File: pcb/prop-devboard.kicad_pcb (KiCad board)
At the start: 4 copper layers, 50.8 x 22.9 mm, 41 parts, among them CN1 STDC14, CN2 SM04B-SRSS-TB (LF)(SN), CN3 ZX-PH2.0-WT2P, CN4 SM04B-SRSS-TB (LF)(SN), J1 Conn_01x12, J2 Conn_01x16, J3 GT-USB-7010ASV, Q1 DMG3415U-7, SW1 SW_Push, U1 STM32G0B1CBT6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

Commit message: Added CubeMX template, and more schematics work
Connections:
- CN1 pad 11: unconnected-(CN1-GNDD-Pad11) -> GND
- CN1 pad 12: unconnected-(CN1-~{RST}-Pad12) -> NRST
- CN1 pad 13: unconnected-(CN1-VCP_RX-Pad13) -> UART_RX
- CN1 pad 14: unconnected-(CN1-VCP_TX-Pad14) -> UART_TX
- CN1 pad 2: unconnected-(CN1-GND-Pad2) -> GND
- CN1 pad 3: unconnected-(CN1-VCC-Pad3) -> +3V3
- CN1 pad 4: unconnected-(CN1-SWDIO-Pad4) -> SWDIO
- CN1 pad 5: unconnected-(CN1-GND-Pad5) -> GND
- CN1 pad 6: unconnected-(CN1-SWCLK-Pad6) -> SWCLK
- CN2 pad 1: unconnected-(CN2-Pad1) -> GND
- CN2 pad 2: unconnected-(CN2-Pad2) -> +3V3
- CN2 pad 3: unconnected-(CN2-Pad3) -> I2C1_SDA
- CN2 pad 4: unconnected-(CN2-Pad4) -> I2C1_SCL
- CN4 pad 1: unconnected-(CN4-Pad1) -> GND
- CN4 pad 2: unconnected-(CN4-Pad2) -> +3V3
- CN4 pad 3: unconnected-(CN4-Pad3) -> I2C2_SDA
- CN4 pad 4: unconnected-(CN4-Pad4) -> I2C2_SCL
- U1 pad 30: unconnected-(U1-PC6-Pad30) -> UART_TX
- U1 pad 31: unconnected-(U1-PC7-Pad31) -> UART_RX

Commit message: Lots of work on schematics
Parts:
- added D2: ESDA7P60-1U1M, prop-devboard:D1610-RD, F.Cu at (115.7, 95.5)
- added D4: ESDALC6V1W5, prop-devboard:SOT-323-5_L2.0-W1.3-LS2.1-BL, F.Cu at (135.4, 85.5)
- moved C10 5.01 mm to (105.8, 70.5)
- moved C6 3.45 mm to (97.4, 66.3)
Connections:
- net Net-(U2-VIN) renamed VIN
- J1 pad 1: unconnected-(J1-Pin_1-Pad1) -> VBAT
- J1 pad 10: unconnected-(J1-Pin_10-Pad10) -> DIGITAL5
- J1 pad 11: unconnected-(J1-Pin_11-Pad11) -> I2C3_SCL
- J1 pad 12: unconnected-(J1-Pin_12-Pad12) -> I2C3_SDA
- J1 pad 2: unconnected-(J1-Pin_2-Pad2) -> VREG_EN
- J1 pad 3: unconnected-(J1-Pin_3-Pad3) -> VBUS
- J1 pad 4: unconnected-(J1-Pin_4-Pad4) -> DIGITAL13
- J1 pad 5: unconnected-(J1-Pin_5-Pad5) -> DIGITAL12
- J1 pad 6: unconnected-(J1-Pin_6-Pad6) -> DIGITAL11
- J1 pad 7: unconnected-(J1-Pin_7-Pad7) -> DIGITAL10
- J1 pad 8: unconnected-(J1-Pin_8-Pad8) -> DIGITAL9
- J1 pad 9: unconnected-(J1-Pin_9-Pad9) -> DIGITAL6
- J2 pad 1: unconnected-(J2-Pin_1-Pad1) -> NRST
- J2 pad 10: unconnected-(J2-Pin_10-Pad10) -> ANALOG5
- J2 pad 11: unconnected-(J2-Pin_11-Pad11) -> SPI_SCK
- J2 pad 12: unconnected-(J2-Pin_12-Pad12) -> SPI_MOSI
- J2 pad 13: unconnected-(J2-Pin_13-Pad13) -> SPI_MISO
- J2 pad 14: unconnected-(J2-Pin_14-Pad14) -> UART_RX
- J2 pad 15: unconnected-(J2-Pin_15-Pad15) -> UART_TX
- J2 pad 16: unconnected-(J2-Pin_16-Pad16) -> BOOT0
- J2 pad 2: unconnected-(J2-Pin_2-Pad2) -> +3V3
- J2 pad 3: unconnected-(J2-Pin_3-Pad3) -> +3V3
- J2 pad 4: unconnected-(J2-Pin_4-Pad4) -> GND
- J2 pad 5: unconnected-(J2-Pin_5-Pad5) -> ANALOG0
- J2 pad 6: unconnected-(J2-Pin_6-Pad6) -> ANALOG1
- J2 pad 7: unconnected-(J2-Pin_7-Pad7) -> ANALOG2
- J2 pad 8: unconnected-(J2-Pin_8-Pad8) -> ANALOG3
- J2 pad 9: unconnected-(J2-Pin_9-Pad9) -> ANALOG4
- R4 pad 1: Net-(U2-EN) -> VREG_EN
- U1 pad 11: unconnected-(U1-PA0-Pad11) -> ANALOG0
- U1 pad 12: unconnected-(U1-PA1-Pad12) -> ANALOG1
- U1 pad 13: unconnected-(U1-PA2-Pad13) -> ANALOG2
- U1 pad 14: unconnected-(U1-PA3-Pad14) -> ANALOG3
- U1 pad 15: unconnected-(U1-PA4-Pad15) -> ANALOG4
- U1 pad 16: unconnected-(U1-PA5-Pad16) -> ANALOG5
- U1 pad 21: unconnected-(U1-PB2-Pad21) -> SPI_MISO
- U1 pad 22: unconnected-(U1-PB10-Pad22) -> SPI_SCK
- U1 pad 23: unconnected-(U1-PB11-Pad23) -> SPI_MOSI
- U1 pad 25: unconnected-(U1-PB13-Pad25) -> I2C2_SCL
- U1 pad 26: unconnected-(U1-PB14-Pad26) -> I2C2_SDA
- U1 pad 29: UART_TX -> I2C1_SCL
- U1 pad 32: UART_RX -> I2C1_SDA
- U1 pad 42: unconnected-(U1-PB3-Pad42) -> I2C3_SCL
- U1 pad 43: unconnected-(U1-PB4-Pad43) -> I2C3_SDA
- U2 pad 3: Net-(U2-EN) -> VREG_EN
- U3 pad 7: BAT_SCL -> I2C3_SCL
- U3 pad 8: BAT_SDA -> I2C3_SDA
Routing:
- added copper zone on B.Cu, net GND
- added copper zone on F.Cu, net GND
- added copper zone on In1.Cu, net GND
- added copper zone on In2.Cu, net GND

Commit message: Mostly finished PCB layout
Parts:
- removed D4: ESDALC6V1W5, prop-devboard:SOT-323-5_L2.0-W1.3-LS2.1-BL
- moved C4 47.1 mm to (125.1, 97.7), turned to -135 degrees
- moved R3 46.0 mm to (130.6, 97.6)
- moved C3 43.1 mm to (121.4, 93.4), turned to 45 degrees
- moved C7 40.0 mm to (127.8, 97.6), turned to 180 degrees
- moved C1 38.1 mm to (113.2, 98.3), turned to 180 degrees
- moved D3 37.9 mm to (104.5, 97.0), turned to 180 degrees
- moved C10 37.3 mm to (134.6, 94.2), turned to 180 degrees
- moved C5 37.2 mm to (121.5, 90.2), turned to 135 degrees
- moved C6 36.3 mm to (118.9, 95.5), turned to -45 degrees
- moved R5 33.5 mm to (110.3, 97.9), turned to 180 degrees
- moved R1 32.6 mm to (108.4, 92.8)
- moved R6 30.8 mm to (116.1, 98.3), turned to 180 degrees
- moved R2 28.7 mm to (108.4, 90.9)
- moved R4 28.5 mm to (116.2, 92.0), turned to 180 degrees
- moved C8 26.9 mm to (108.4, 88.7)
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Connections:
- CN1 pad 6: SWCLK -> BOOT0
- U1 pad 33: unconnected-(U1-PA9/PA11-Pad33) -> DIGITAL5
- U1 pad 34: unconnected-(U1-PA10/PA12-Pad34) -> DIGITAL6
- U1 pad 36: SWCLK -> BOOT0
- U1 pad 37: unconnected-(U1-PA15-Pad37) -> DIGITAL9
- U1 pad 38: unconnected-(U1-PD0-Pad38) -> DIGITAL10
- U1 pad 39: unconnected-(U1-PD1-Pad39) -> DIGITAL11
- U1 pad 40: unconnected-(U1-PD2-Pad40) -> DIGITAL12
- U1 pad 41: unconnected-(U1-PD3-Pad41) -> DIGITAL13
- U4 pad 9: unconnected-(U4-EP-Pad9) -> GND
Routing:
- net +3V3: track 0.00 -> 76.6 mm, vias 0 -> 7
- net NRST: track 0.00 -> 49.3 mm, vias 0 -> 3
- net VBUS: track 0.00 -> 49.0 mm, vias 0 -> 2
- net GND: track 0.00 -> 39.9 mm, vias 0 -> 30
- net I2C3_SDA: track 0.00 -> 34.9 mm, vias 0 -> 3
- net BOOT0: track 0.00 -> 31.7 mm, vias 0 -> 3
- net I2C3_SCL: track 0.00 -> 31.1 mm, vias 0 -> 4
- net VBAT: track 0.00 -> 30.7 mm, vias 0 -> 2
- net UART_RX: track 0.00 -> 29.3 mm
- net UART_TX: track 0.00 -> 26.4 mm, vias 0 -> 2
- net I2C2_SCL: track 0.00 -> 19.7 mm, vias 0 -> 2
- net I2C2_SDA: track 0.00 -> 19.5 mm, vias 0 -> 2
- net I2C1_SDA: track 0.00 -> 19.0 mm, vias 0 -> 2
- net SWDIO: track 0.00 -> 17.2 mm, vias 0 -> 2
- net I2C1_SCL: track 0.00 -> 17.1 mm, vias 0 -> 2
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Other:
- board text added: "CHRG"
- board text added: "RESET"

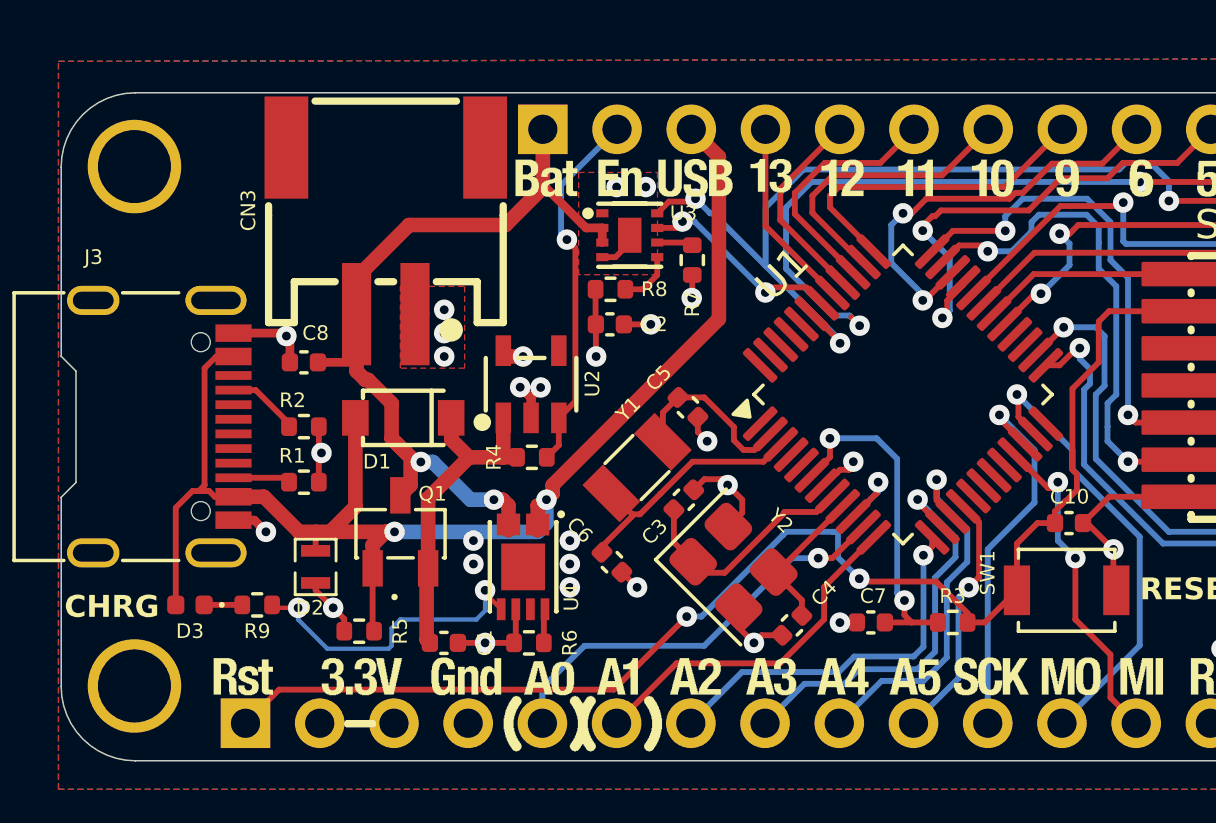
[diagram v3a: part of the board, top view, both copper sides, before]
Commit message: Added USB support
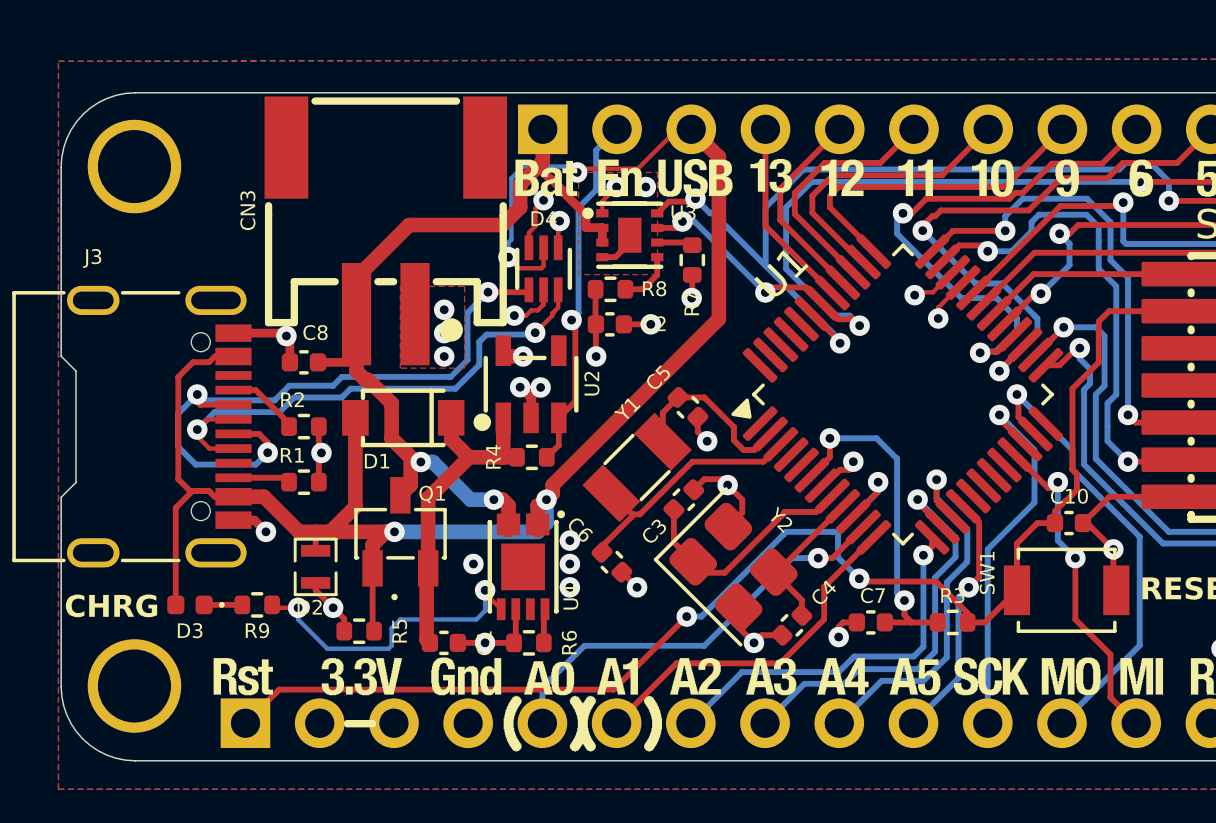
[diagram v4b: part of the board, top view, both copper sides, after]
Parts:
- added D4: USBLC6-2P6, prop-devboard:SOT-666-6_L1.6-W1.2-P0.50-LS1.6-BR, F.Cu at (116.6, 85.5)
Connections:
- J3 pad A6: unconnected-(J3-D+-PadA6) -> Net-(D4-I/O2-Pad3)
- J3 pad A7: unconnected-(J3-D--PadA7) -> Net-(D4-I/O1-Pad1)
- J3 pad B6: unconnected-(J3-D+-PadB6) -> Net-(D4-I/O2-Pad3)
- J3 pad B7: unconnected-(J3-D--PadB7) -> Net-(D4-I/O1-Pad1)
- U1 pad 27: unconnected-(U1-PB15-Pad27) -> DIGITAL5
- U1 pad 28: unconnected-(U1-PA8-Pad28) -> DIGITAL6
- U1 pad 33: DIGITAL5 -> USB_DM
- U1 pad 34: DIGITAL6 -> USB_DP
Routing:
- net Net-(D4-I/O1-Pad1): track 0.00 -> 22.7 mm, vias 0 -> 3
- net USB_DM: track 0.00 -> 21.2 mm, vias 0 -> 2
- net USB_DP: track 0.00 -> 18.6 mm, vias 0 -> 2
- net Net-(D4-I/O2-Pad3): track 0.00 -> 18.3 mm, vias 0 -> 2
- net VBUS: track 49.0 -> 61.9 mm, vias 2 -> 4
- net DIGITAL6: track 14.2 -> 18.7 mm
- net DIGITAL5: track 16.4 -> 20.2 mm
- net GND: track 39.9 -> 43.6 mm
- net I2C3_SCL: track 31.1 -> 32.7 mm
